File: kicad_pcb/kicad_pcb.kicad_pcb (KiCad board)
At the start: 2 copper layers, 36 x 21 mm, 18 parts, among them IC1 LM358DR2G, IC2 MCP4725A0T-E_CH, IC3 L78M24ACDT-TR

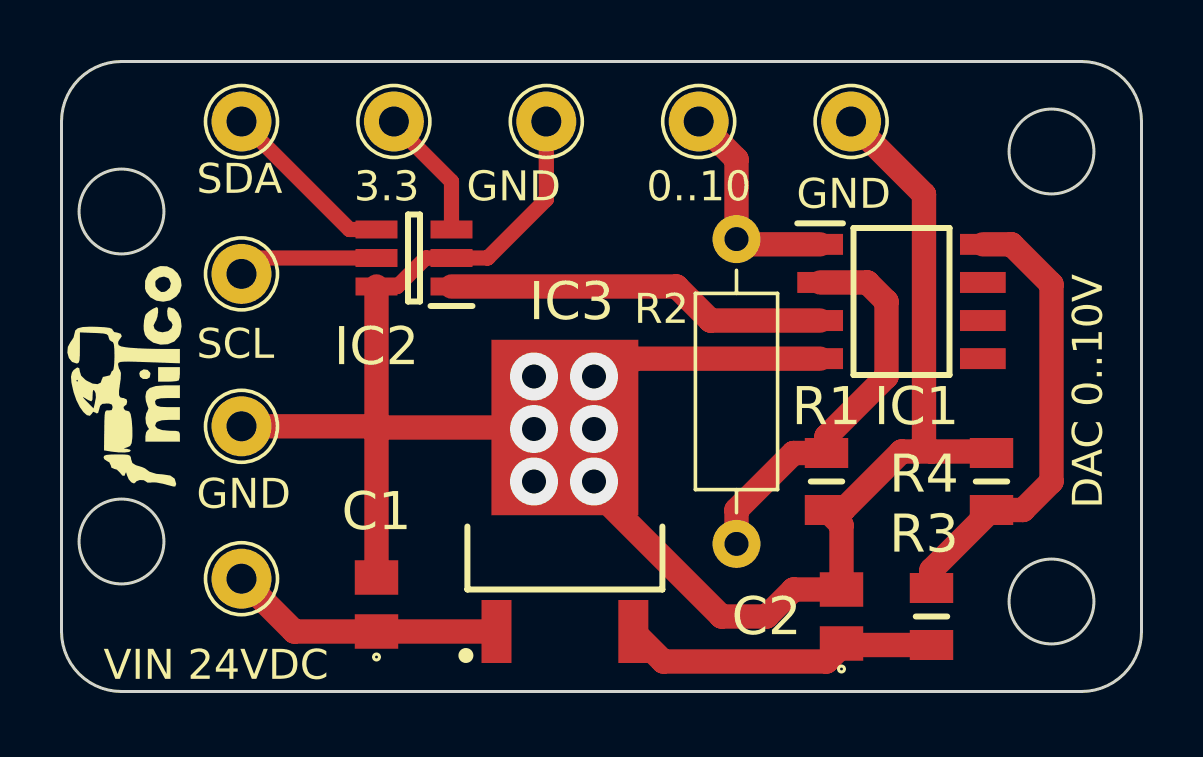
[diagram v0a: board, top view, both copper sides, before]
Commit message: 20.3k rsistor update
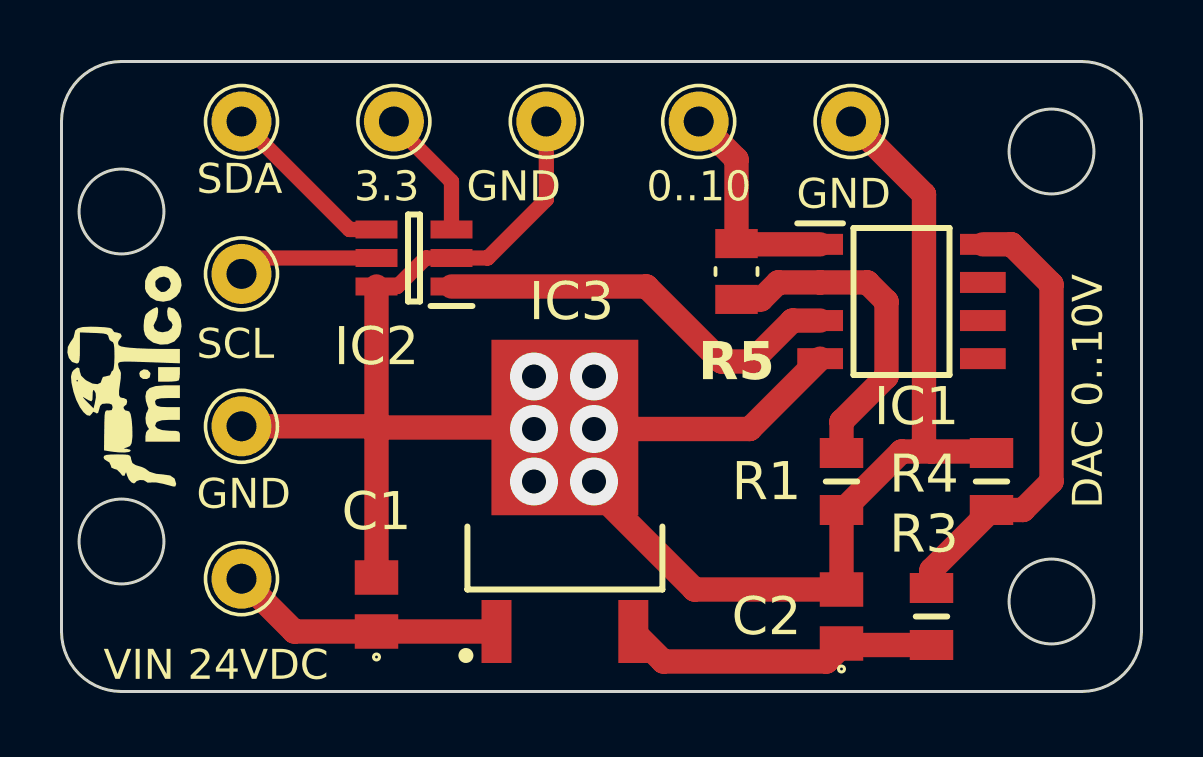
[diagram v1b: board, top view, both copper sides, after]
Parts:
- removed R2: 20.3k 0.1%, Resistor_THT:R_Axial_DIN0207_L6.3mm_D2.5mm_P10.16mm_Horizontal
- added R5: 20.3k 0.1%, Snapeda:TNPW080520K3BEEA_RESC2012X55N, F.Cu at (133.5, 78.0)
- moved R1 0.50 mm to (137.0, 85.0)
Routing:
- net Net-(IC1-INPUTS_A_1): track 13.3 -> 11.2 mm
- net Net-(IC1-INPUTS_A_2): track 12.8 -> 13.9 mm

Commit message: 20.3k resistor update to KOA
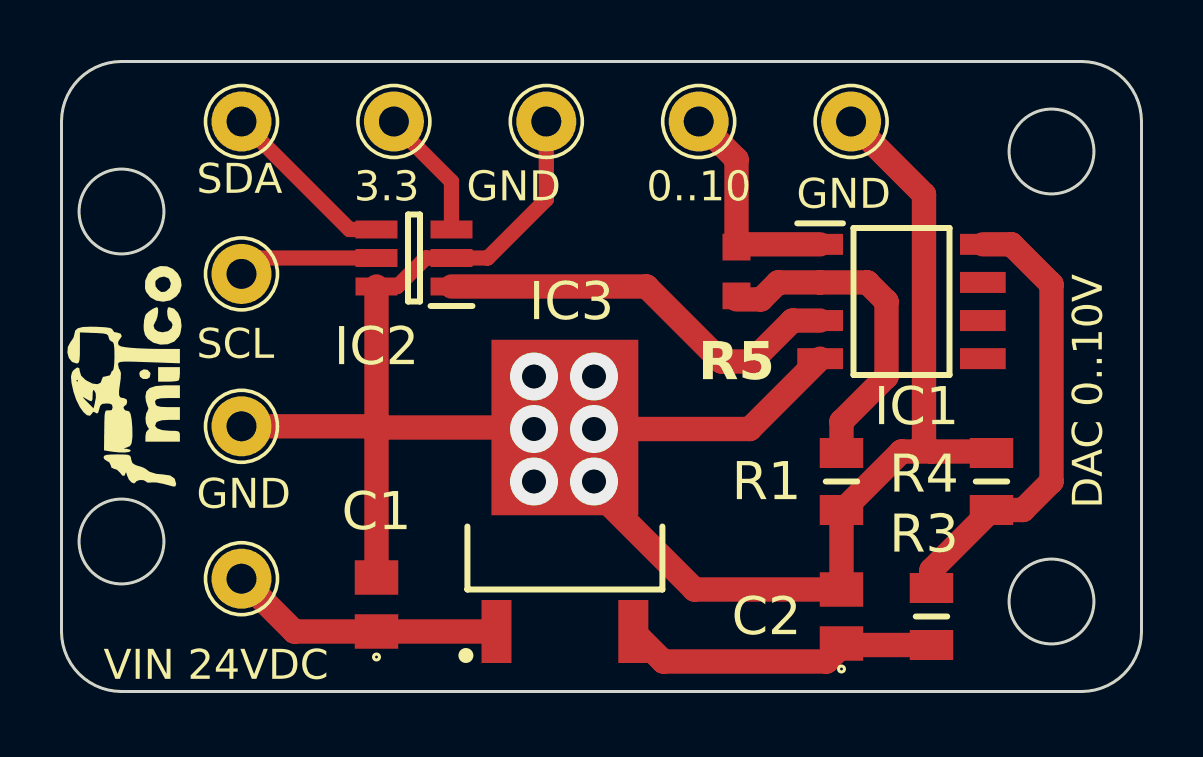
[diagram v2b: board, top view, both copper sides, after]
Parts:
- R5: footprint Snapeda:TNPW080520K3BEEA_RESC2012X55N -> Snapeda:RN73H1JTTD2032B25_RESC1608X55N
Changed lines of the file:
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@@
 		)
 	)
-	(footprint "Snapeda:TNPW080520K3BEEA_RESC2012X55N"
+	(footprint "Snapeda:RN73H1JTTD2032B25_RESC1608X55N"
 		(layer "F.Cu")
 		(at 133.5 78 90)
 		(property "Reference" "R5"
-			(at -3 0 0)
+			(at -3 0 180)
 			(layer "F.SilkS")
 			(effects
@@
 		)
 		(property "Value" "20.3k 0.1%"
-			(at 1.34 1.3 270)
+			(at 1.49 1.05 90)
 			(layer "F.Fab")
 			(effects
@@
 			)
 		)
-		(property "Footprint" "Snapeda:TNPW080520K3BEEA_RESC2012X55N"
+		(property "Footprint" "Snapeda:RN73H1JTTD2032B25_RESC1608X55N"
 			(at 0 0 90)
 			(unlocked yes)
@@
 			)
 		)
-		(property "MF" "Vishay Dale"
-			(at 0 0 90)
-			(unlocked yes)
-			(layer "F.Fab")
-			(hide yes)
-			(effects
-				(font
-					(size 1 1)
-					(thickness 0.15)
-				)
-			)
-		)
-		(property "Description_1" "\n20.3 kOhms ±0.1% 0.26W Chip Resistor 0805 (2012 Metric) Anti-Sulfur, Automotive AEC-Q200, Moisture Resistant Thin Film\n"
-			(at 0 0 90)
-			(unlocked yes)
-			(layer "F.Fab")
-			(hide yes)
-			(effects
-				(font
-					(size 1 1)
-					(thickness 0.15)
-				)
-			)
-		)
-		(property "Package" "2012 Vishay"
+		(property "MF" "KOA Speer"
+			(at 0 0 90)
+			(unlocked yes)
+			(layer "F.Fab")
+			(hide yes)
+			(effects
+				(font
+					(size 1 1)
+					(thickness 0.15)
+				)
+			)
+		)
+		(property "Description_1" "\n20.3 kOhms ±0.1% 0.1W, 1/10W Chip Resistor 0603 (1608 Metric) Automotive AEC-Q200, Moisture Resistant Metal Film\n"
+			(at 0 0 90)
+			(unlocked yes)
+			(layer "F.Fab")
+			(hide yes)
+			(effects
+				(font
+					(size 1 1)
+					(thickness 0.15)
+				)
+			)
+		)
+		(property "Package" "603 KOA"
 			(at 0 0 90)
 			(unlocked yes)
@@
 			)
 		)
-		(property "SnapEDA_Link" "https://www.snapeda.com/parts/TNPW080520K3BEEA/Vishay+Dale/view-part/?ref=snap"
-			(at 0 0 90)
-			(unlocked yes)
-			(layer "F.Fab")
-			(hide yes)
-			(effects
-				(font
-					(size 1 1)
-					(thickness 0.15)
-				)
-			)
-		)
-		(property "MP" "TNPW080520K3BEEA"
+		(property "SnapEDA_Link" "https://www.snapeda.com/parts/RN73H1JTTD2032B25/KOA+Speer/view-part/?ref=snap"
+			(at 0 0 90)
+			(unlocked yes)
+			(layer "F.Fab")
+			(hide yes)
+			(effects
+				(font
+					(size 1 1)
+					(thickness 0.15)
+				)
+			)
+		)
+		(property "MP" "RN73H1JTTD2032B25"
 			(at 0 0 90)
 			(unlocked yes)
@@
 			)
 		)
-		(property "Check_prices" "https://www.snapeda.com/parts/TNPW080520K3BEEA/Vishay+Dale/view-part/?ref=eda"
-			(at 0 0 90)
-			(unlocked yes)
-			(layer "F.Fab")
-			(hide yes)
-			(effects
-				(font
-					(size 1 1)
-					(thickness 0.15)
-				)
-			)
-		)
+		(property "Check_prices" "https://www.snapeda.com/parts/RN73H1JTTD2032B25/KOA+Speer/view-part/?ref=eda"
+			(at 0 0 90)
+			(unlocked yes)
+			(layer "F.Fab")
+			(hide yes)
+			(effects
+				(font
+					(size 1 1)
+					(thickness 0.15)
+				)
+			)
+		)
+		(sheetname "Root")
+		(sheetfile "kicad_pcb.kicad_sch")
 		(attr smd)
 		(fp_line
-			(start -0.12 -0.7)
-			(end 0.12 -0.7)
-			(stroke
-				(width 0.127)
-				(type solid)
-			)
-			(layer "F.SilkS")
-		)
-		(fp_line
-			(start -0.12 0.7)
-			(end 0.12 0.7)
-			(stroke
-				(width 0.127)
-				(type solid)
-			)
-			(layer "F.SilkS")
-		)
-		(fp_line
-			(start -1.665 -0.96)
-			(end 1.665 -0.96)
-			(stroke
-				(width 0.05)
-				(type solid)
-			)
-			(layer "F.CrtYd")
-		)
-		(fp_line
-			(start 1.665 0.96)
-			(end 1.665 -0.96)
-			(stroke
-				(width 0.05)
-				(type solid)
-			)
-			(layer "F.CrtYd")
-		)
-		(fp_line
-			(start -1.665 0.96)
-			(end -1.665 -0.96)
-			(stroke
-				(width 0.05)
-				(type solid)
-			)
-			(layer "F.CrtYd")
-		)
-		(fp_line
-			(start -1.665 0.96)
-			(end 1.665 0.96)
-			(stroke
-				(width 0.05)
-				(type solid)
-			)
-			(layer "F.CrtYd")
-		)
-		(fp_line
-			(start 1.05 -0.7)
-			(end -1.05 -0.7)
-			(stroke
-				(width 0.127)
-				(type solid)
-			)
-			(layer "F.Fab")
-		)
-		(fp_line
-			(start 1.05 0.7)
-			(end 1.05 -0.7)
-			(stroke
-				(width 0.127)
-				(type solid)
-			)
-			(layer "F.Fab")
-		)
-		(fp_line
-			(start 1.05 0.7)
-			(end -1.05 0.7)
-			(stroke
-				(width 0.127)
-				(type solid)
-			)
-			(layer "F.Fab")
-		)
-		(fp_line
-			(start -1.05 0.7)
-			(end -1.05 -0.7)
+			(start -1.508 -0.715)
+			(end 1.508 -0.715)
+			(stroke
+				(width 0.05)
+				(type solid)
+			)
+			(layer "F.CrtYd")
+		)
+		(fp_line
+			(start 1.508 0.715)
+			(end 1.508 -0.715)
+			(stroke
+				(width 0.05)
+				(type solid)
+			)
+			(layer "F.CrtYd")
+		)
+		(fp_line
+			(start -1.508 0.715)
+			(end -1.508 -0.715)
+			(stroke
+				(width 0.05)
+				(type solid)
+			)
+			(layer "F.CrtYd")
+		)
+		(fp_line
+			(start -1.508 0.715)
+			(end 1.508 0.715)
+			(stroke
+				(width 0.05)
+				(type solid)
+			)
+			(layer "F.CrtYd")
+		)
+		(fp_line
+			(start 0.9 -0.45)
+			(end -0.9 -0.45)
+			(stroke
+				(width 0.127)
+				(type solid)
+			)
+			(layer "F.Fab")
+		)
+		(fp_line
+			(start 0.9 0.45)
+			(end 0.9 -0.45)
+			(stroke
+				(width 0.127)
+				(type solid)
+			)
+			(layer "F.Fab")
+		)
+		(fp_line
+			(start 0.9 0.45)
+			(end -0.9 0.45)
+			(stroke
+				(width 0.127)
+				(type solid)
+			)
+			(layer "F.Fab")
+		)
+		(fp_line
+			(start -0.9 0.45)
+			(end -0.9 -0.45)
 			(stroke
 				(width 0.127)
@@
 		)
 		(pad "1" smd rect
-			(at -0.93 0 90)
-			(size 0.97 1.42)
+			(at -0.814 0 90)
+			(size 0.89 0.93)
 			(layers "F.Cu" "F.Paste" "F.Mask")
 			(net 5 "Net-(IC1-INPUTS_A_1)")
@@
 		)
 		(pad "2" smd rect
-			(at 0.93 0 90)
-			(size 0.97 1.42)
+			(at 0.814 0 90)
+			(size 0.89 0.93)
 			(layers "F.Cu" "F.Paste" "F.Mask")
 			(net 4 "Net-(IC1-OUTPUT_A)")
@@
 			(solder_mask_margin 0.102)
 		)
-		(model "${KICAD_3RD_PARTY}/Snapeda.3dshapes/TNPW080520K3BEEA.step"
+		(model "${KICAD_3RD_PARTY}/Snapeda.3dshapes/RN73H1JTTD2032B25.step"
 			(offset
 				(xyz 0 0 0)
